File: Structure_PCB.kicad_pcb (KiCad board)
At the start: 2 copper layers, 180 x 100 mm, 137 parts, among them J10 JST-GH 4Pin, J11 JST-GH 4Pin, J12 JST-GH 4Pin, J6 6620XX236022_662004236022, J9 Conn_02x04_Top_Bottom, K2 FINDER-40.61

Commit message: updated StructurePcB
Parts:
- removed D4, D5, D6: ~, Diode_SMD:D_SOD-123F
- removed F1: 100 mA, Fuse:Fuse_1206_3216Metric_Pad1.42x1.75mm_HandSolder
- removed HS10, HS100, HS101, HS102, HS103, HS104, HS105, HS106, HS107, HS108, HS109, HS11, HS110, HS111, HS112, HS113, HS114, HS115, HS116, HS117, HS118, HS119, HS12, HS120, HS13, HS14, HS15, HS16, HS17, HS18, HS19, HS20, HS21, HS22, HS23, HS24, HS25, HS26, HS27, HS28, HS29, HS30, HS31, HS32, HS33, HS34, HS35, HS36, HS37, HS42, HS43, HS44, HS45, HS46, HS47, HS48, HS49, HS50, HS51, HS52, HS53, HS54, HS55, HS56, HS57, HS58, HS59, HS60, HS61, HS62, HS63, HS64, HS65, HS66, HS67, HS68, HS69, HS70, HS71, HS72, HS73, HS74, HS75, HS76, HS77, HS78, HS79, HS80, HS81, HS82, HS83, HS84, HS85, HS86, HS87, HS88, HS89, HS9, HS90, HS91, HS92, HS93, HS94, HS95, HS96, HS97, HS98, HS99: Heatsink_Pad, Heatsink:würth 5x5 heat pads
- removed J10, J11, J12: JST-GH 4Pin, Connector_JST:JST_GH_SM04B-GHS-TB_1x04-1MP_P1.25mm_Horizontal
- removed J6: 6620XX236022_662004236022, stigma:Molex_Micro-Fit_3.0_43045-0400_2x02_P3.00mm_Horizontal
- removed J9: Conn_02x04_Top_Bottom, Connector_Molex:Molex_Micro-Fit_3.0_43045-0800_2x04_P3.00mm_Horizontal
- removed K2: FINDER-40.61, Relay_THT:Relay_SPDT_Finder_40.61
- added ArmingBoard: MountingHole_Pad, Mounting_Wuerth:Mounting_Wuerth_WA-SMSR-3.2mm_H4.6mm_ReverseMount_9775046960, F.Cu at (59.5, 65.2)
- added ArmingBoard: MountingHole_Pad, Mounting_Wuerth:Mounting_Wuerth_WA-SMSR-3.2mm_H4.6mm_ReverseMount_9775046960, F.Cu at (59.4, 98.3)
- added ArmnigBoard: MountingHole_Pad, Mounting_Wuerth:Mounting_Wuerth_WA-SMSR-3.2mm_H4.6mm_ReverseMount_9775046960, F.Cu at (88.0, 65.4)
- moved H3 81.5 mm to (207.7, 59.2)
- moved H4 69.0 mm to (207.7, 127.2)
- moved H1 61.3 mm to (127.7, 127.2)
- moved H2 60.9 mm to (127.7, 59.2)
- moved H5 13.1 mm to (205.8, 88.1)
- moved H6 13.1 mm to (205.8, 138.1)
- moved H7 13.1 mm to (110.8, 138.1)
- moved H8 13.1 mm to (110.8, 88.1)
- moved H13 9.74 mm to (109.8, 99.5)
- moved H14 9.74 mm to (169.8, 99.5)
- moved H15 9.74 mm to (169.8, 126.5)
- moved H19 9.25 mm to (218.0, 85.9)
- moved H18 9.24 mm to (218.0, 128.9)
- moved H16 9.22 mm to (85.0, 128.9)
- moved H17 9.16 mm to (84.9, 85.9)
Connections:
- H1 pad 1: GND -> unconnected-(H1-Pad1)
- H10 pad 1: GND -> unconnected-(H10-Pad1)
- H11 pad 1: GND -> unconnected-(H11-Pad1)
- H12 pad 1: GND -> unconnected-(H12-Pad1)
- H13 pad 1: GND -> unconnected-(H13-Pad1)_2
- H14 pad 1: GND -> unconnected-(H14-Pad1)
- H15 pad 1: GND -> unconnected-(H15-Pad1)_1
- H16 pad 1: GND -> unconnected-(H16-Pad1)_3
- H17 pad 1: GND -> unconnected-(H17-Pad1)
- H18 pad 1: GND -> unconnected-(H18-Pad1)_2
- H19 pad 1: GND -> unconnected-(H19-Pad1)_2
- H2 pad 1: GND -> unconnected-(H2-Pad1)_2
- H3 pad 1: GND -> unconnected-(H3-Pad1)_1
- H4 pad 1: GND -> unconnected-(H4-Pad1)_3
- H5 pad 1: GND -> unconnected-(H5-Pad1)
- H6 pad 1: GND -> unconnected-(H6-Pad1)_3
- H7 pad 1: GND -> unconnected-(H7-Pad1)_1
- H8 pad 1: GND -> unconnected-(H8-Pad1)_3
- H9 pad 1: GND -> unconnected-(H9-Pad1)
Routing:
- net /SBout: track 219.8 -> 0.00 mm
- net /post_arm: track 102.3 -> 0.00 mm
- net /pre_fuse: track 15.4 -> 0.00 mm
- net /SBin: track 12.6 -> 0.00 mm
- net GND: track 7.53 -> 0.00 mm, vias 560 -> 0
- net /PBin: track 6.78 -> 0.00 mm, vias 2 -> 0
- net (no net): track 0.00 -> 3.50 mm, vias 1 -> 0
- removed copper zone on F.Cu, net /HCin
- removed copper zone on B.Cu, net /HCout
- removed copper zone on B.Cu, net /PBin
- removed copper zone on F.Cu, net /SBin
- removed copper zone on F.Cu, net /SBout
- removed copper zone on B.Cu, net GND
- removed copper zone on F.Cu, net GND
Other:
- outline, holes or cut-outs redrawn
- board text added: "1 2 3"
- board text added: "Arming Board (Back)"
- board text added: "Batteryboard"
- board text added: "Batteryboard (Back)"
- board text added: "Engine Board"
- board text added: "EngineBoard"
- board text added: "FLightComp"
- board text added: "Flight Computer"
- board text added: "FlightComp"
- board text added: "Flightcomp"
- board text added: "Mounting"
- board text added: "status leds"
- board text removed: "EB"
- board text removed: "FC"
- board text removed: "PB power in"
- board text removed: "c.d."
- board text removed: "c.i.p."
- board text removed: "pw.+"
- board text removed: "s 0 s 1 s 2"

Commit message: Add files via upload
updated the structure PCB to fit Arming and Batteryboard
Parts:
- removed H16, H17, H18, H19: MountingHole_Pad, Mounting_Wuerth:Mounting_Wuerth_WA-SMSR-3.2mm_H4.6mm_ReverseMount_9775046960
- added H23: MountingHole_Pad, Mounting_Wuerth:Mounting_Wuerth_WA-SMSR-3.2mm_H4.6mm_ReverseMount_9775046960, F.Cu at (90.1, 58.6)
- moved H22 32.5 mm to (90.1, 87.6), turned to 90 degrees
- moved H21 30.6 mm to (58.1, 58.6), turned to 90 degrees
- moved H20 22.4 mm to (58.1, 87.6), turned to 90 degrees
- moved H5 16.6 mm to (204.2, 71.6)
- moved H6 16.6 mm to (204.2, 121.6)
- moved H7 16.6 mm to (109.2, 121.6)
- moved H8 16.6 mm to (109.2, 71.6)
- moved H1 14.0 mm to (115.7, 134.4)
- moved H2 14.0 mm to (115.7, 66.4)
- moved H3 14.0 mm to (195.7, 66.4)
- moved H4 14.0 mm to (195.7, 134.4)
- moved H14 13.8 mm to (165.4, 86.5)
- moved H15 13.8 mm to (165.4, 113.5)
- moved H13 13.8 mm to (105.5, 86.5)
- renumbered ArmingBoard to H20, ArmnigBoard to H21, ArmingBoard to H22
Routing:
- net (no net): track 3.50 -> 0.00 mm
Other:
- outline, holes or cut-outs redrawn
- board text added: "Powerboard (Back)"
- board text added: "Switch cutout"
- board text added: "flightcomp antenna"
- board text added: "powerboard"
- board text removed: "Batteryboard"
- board text removed: "Batteryboard (Back)"

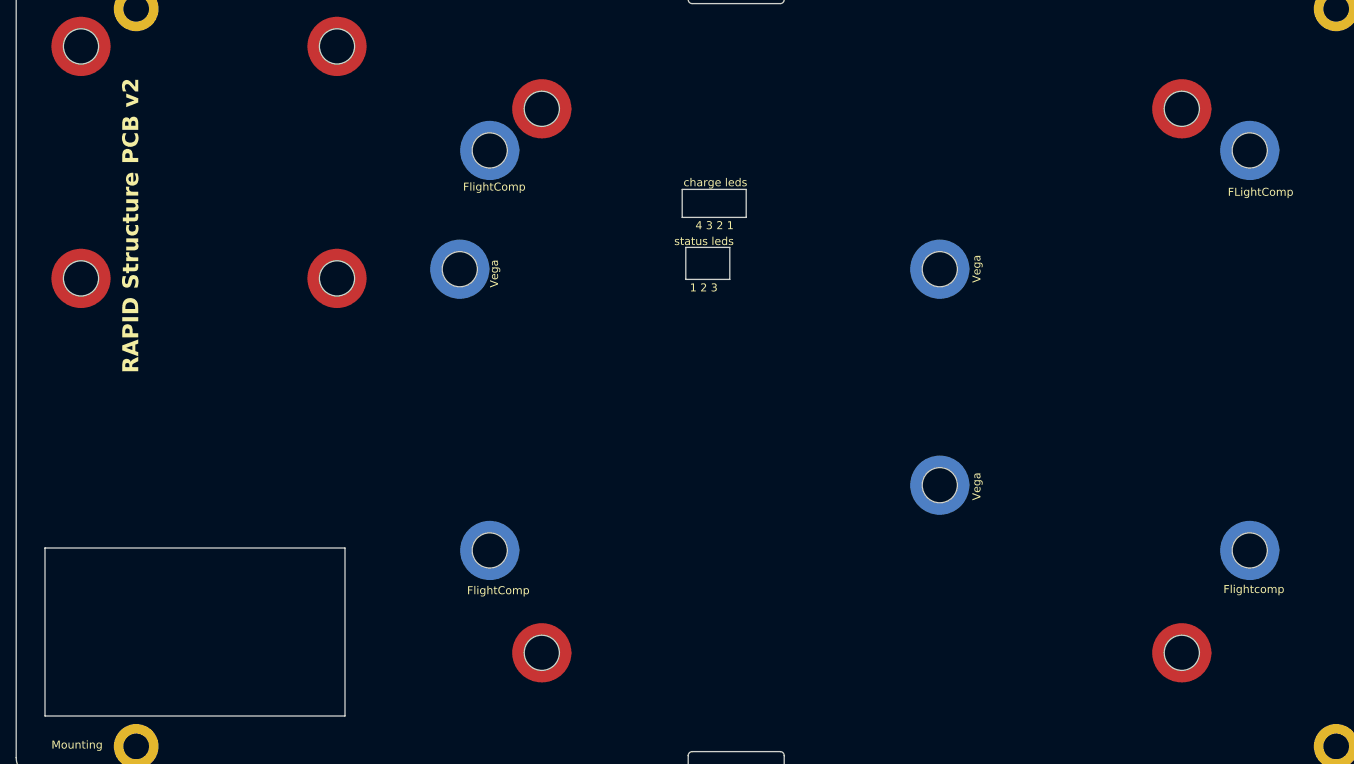
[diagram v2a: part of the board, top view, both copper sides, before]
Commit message: Add files via upload
Added new switch cutout and Silkscreen
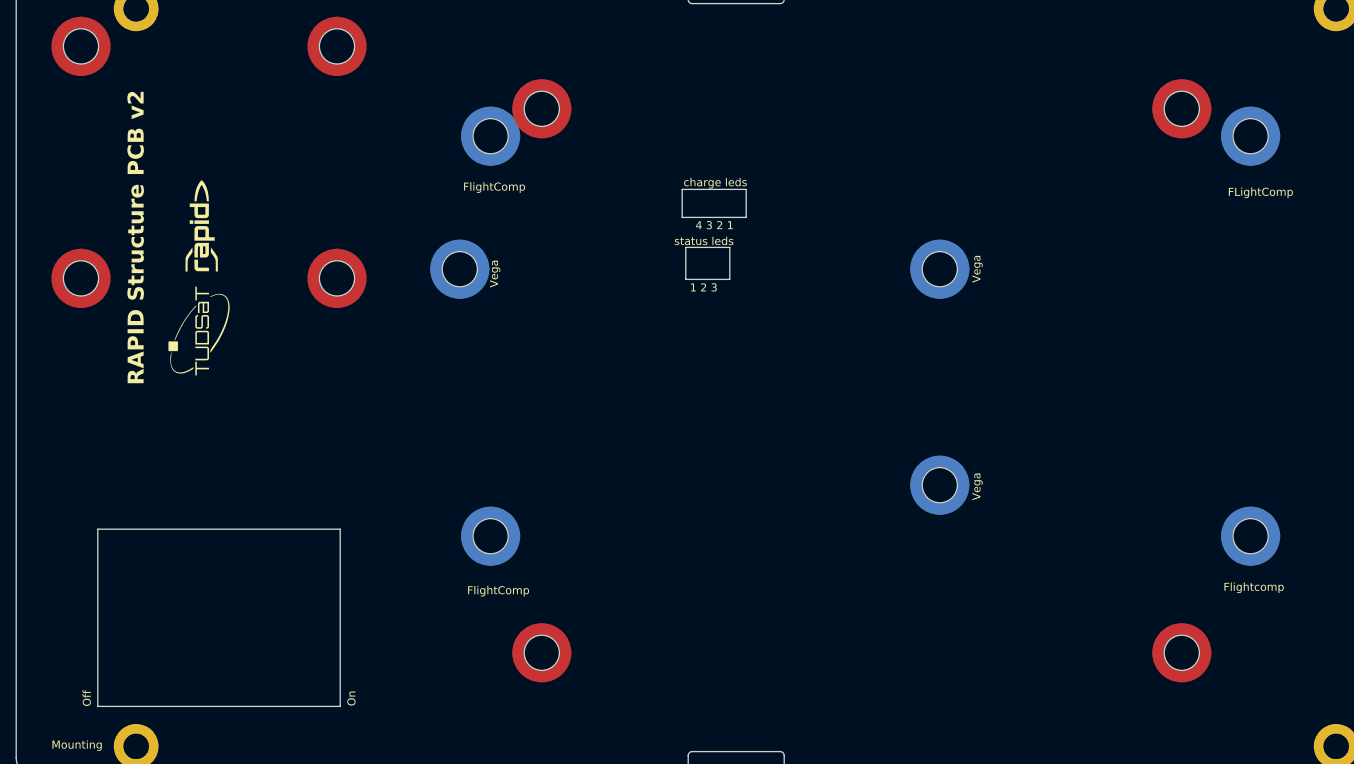
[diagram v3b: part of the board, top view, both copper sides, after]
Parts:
- added G***: LOGO, frodo_io_module:rapid_logo, F.Cu at (73.2, 81.0)
- moved H5 1.78 mm to (204.3, 69.8)
- moved H6 1.78 mm to (204.3, 119.8)
- moved H7 1.78 mm to (109.3, 119.8)
- moved H8 1.78 mm to (109.3, 69.8)
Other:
- outline, holes or cut-outs redrawn
- board text added: "Armingboard"
- board text added: "Batteryboard"
- board text added: "Batteryboard (Back)"
- board text added: "Off"
- board text added: "On"
- board text removed: "Powerboard (Back)"
- board text removed: "powerboard"

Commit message: Add files via upload
fixed positioning of LED cutouts
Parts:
- moved G*** 106.4 mm to (160.8, 141.4), turned to 0 degrees
- moved H4 4.49 mm to (199.3, 131.8)
- moved H3 4.45 mm to (199.3, 63.8)
- moved H2 3.01 mm to (114.2, 63.8)
- moved H1 2.93 mm to (114.4, 131.8)
- moved H22 2.10 mm to (92.0, 88.5)
- moved H21 2.10 mm to (60.0, 59.5)
- moved H23 2.10 mm to (92.0, 59.5)
- moved H20 2.10 mm to (60.0, 88.5)
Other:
- outline, holes or cut-outs redrawn
- board text added: "3 2 1"
- board text added: "Powerboard"
- board text added: "Powerboard (Back)"
- board text removed: "1 2 3"
- board text removed: "Batteryboard"
- board text removed: "Batteryboard (Back)"

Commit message: changed footprint and placement of armingboard
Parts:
- H20, H21, H22, H23: footprint Mounting_Wuerth:Mounting_Wuerth_WA-SMSR-3.2mm_H4.6mm_ReverseMount_9775046960 -> MountingHole:MountingHole_3.2mm_M3_DIN965_Pad_TopBottom
- moved H3 12.8 mm to (212.1, 63.4)
- moved H1 12.8 mm to (127.2, 131.4)
- moved H2 12.8 mm to (127.0, 63.4)
- moved H4 12.8 mm to (212.1, 131.4)
- moved H22 9.01 mm to (94.9, 97.0)
- moved H20 8.74 mm to (60.5, 97.2)
- moved H23 4.40 mm to (95.1, 62.6)
- moved H21 3.16 mm to (60.5, 62.6)
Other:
- outline, holes or cut-outs redrawn

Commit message: improve silkscreen, center fc and fix mounting holes
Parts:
- H20, H21, H22, H23: footprint MountingHole:MountingHole_3.2mm_M3_DIN965_Pad_TopBottom -> Mounting_Wuerth:Mounting_Wuerth_WA-SMSR-3.2mm_H4.6mm_ReverseMount_9775046960
- moved H11 10.1 mm to (55.0, 55.0)
- moved H10 10.1 mm to (55.0, 145.0)
- moved H23 5.36 mm to (92.0, 67.0)
- moved H21 5.04 mm to (58.0, 67.0)
- moved H22 4.92 mm to (92.0, 101.0)
- moved H20 4.53 mm to (58.0, 101.0)
- moved H5 3.59 mm to (204.3, 73.4)
- moved H6 3.59 mm to (204.3, 123.4)
- moved H7 3.59 mm to (109.3, 123.4)
- moved H8 3.59 mm to (109.3, 73.4)
- moved H1 2.19 mm to (125.0, 131.0)
- moved H4 2.18 mm to (210.0, 131.0)
- moved H3 2.16 mm to (210.0, 63.0)
- moved H2 2.04 mm to (125.0, 63.0)
- moved H12 1.10 mm to (215.0, 55.0)
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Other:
- outline, holes or cut-outs redrawn
- board text added: "@TODO fix mounting holes"
- board text added: "FC"
- board text added: "min. >5mm"
- board text removed: "Engine Board"
- board text removed: "EngineBoard"
- board text removed: "FLightComp"
- board text removed: "FlightComp"
- board text removed: "Flightcomp"
- board text removed: "Mounting"

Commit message: order version
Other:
- board text removed: "MB Mounting 4 holes 50x95"
- board text removed: "PB Mounting 4 holes 72x115 tbd!"
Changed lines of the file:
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@@
-		)
-	)
-	(gr_text "MB Mounting 4 holes 50x95"
-		(at 34.6 21.5 0)
-		(layer "Cmts.User")
-		(effects
-			(font
-				(size 1 1)
-				(thickness 0.15)
-			)
-			(justify left bottom)
-		)
-	)
-	(gr_text "PB Mounting 4 holes 72x115 tbd!"
-		(at 34.8 24.2 0)
-		(layer "Cmts.User")
-		(effects
-			(font
-				(size 1 1)
-				(thickness 0.15)
-			)
-			(justify left bottom)
 		)
 	)
